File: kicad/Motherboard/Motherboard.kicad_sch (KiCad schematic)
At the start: 64 parts, among them J1 USB_C_Receptacle_USB2.0, J2 Conn_01x16_Pin, J3 Conn_01x16_Pin, J4 Conn_01x16_Pin, J5 Conn_01x02_Pin, J6 Conn_01x04_Pin, J7 Conn_01x04_Pin, J8 Conn_01x16_Pin, J9 Conn_01x02_Pin, Q1 DMN3404L, SW1 Reset, SW2 Boot, U1 ESP32-S2-SOLO, U2 LD1117S33TR_SOT223, U3 CD74HC4067M, U4 CD74HC4067M, U5 CD74HC4067M, U6 CD74HC4067M, U7 TMC2208-LA, U8 TMC2208-LA, U9 LM2575-5.0BT

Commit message: final schematic
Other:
- moved on the sheet: TP1
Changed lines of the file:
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@@
 	)
 	(junction
+		(at 30.48 176.53)
+		(diameter 0)
+		(color 0 0 0 0)
+	)
+	(junction
 		(at 81.28 148.59)
 		(diameter 0)
@@
 	)
 	(junction
-		(at 34.29 176.53)
-		(diameter 0)
-		(color 0 0 0 0)
-	)
-	(junction
 		(at 87.63 148.59)
 		(diameter 0)
@@
 	(wire
 		(pts
-			(xy 34.29 176.53) (xy 35.56 176.53)
-		)
-		(stroke
-			(width 0)
-			(type default)
-		)
-	)
-	(wire
-		(pts
 			(xy 92.71 177.8) (xy 96.52 177.8)
 		)
@@
 	(wire
 		(pts
-			(xy 29.21 176.53) (xy 34.29 176.53)
+			(xy 29.21 176.53) (xy 30.48 176.53)
 		)
 		(stroke
@@
 	(wire
 		(pts
+			(xy 30.48 176.53) (xy 35.56 176.53)
+		)
+		(stroke
+			(width 0)
+			(type default)
+		)
+	)
+	(wire
+		(pts
 			(xy 191.77 27.94) (xy 191.77 29.21)
 		)
@@
 		(on_board yes)
 		(dnp no)
-		(fields_autoplaced yes)
 		(property "Reference" "TP2"
-			(at 118.11 173.2279 0)
+			(at 113.792 172.466 0)
 			(effects
 				(font
@@
 		)
 		(property "Value" "12VConverter_TestPoint"
-			(at 118.11 175.7679 0)
+			(at 100.33 170.434 0)
 			(effects
 				(font
@@
 		(dnp no)
 		(property "Reference" "D2"
-			(at 137.16 176.53 90)
+			(at 143.256 175.514 0)
 			(effects
 				(font
@@
 		)
 		(property "Value" "1N5819"
-			(at 145.542 180.848 0)
+			(at 147.066 174.498 90)
 			(effects
 				(font
@@
 		(on_board yes)
 		(dnp no)
-		(fields_autoplaced yes)
 		(property "Reference" "TP3"
-			(at 138.43 176.0219 0)
+			(at 134.112 179.578 0)
 			(effects
 				(font
@@
 		)
 		(property "Value" "BeforeEM_TestPoint"
-			(at 138.43 178.5619 0)
+			(at 126.492 181.61 0)
 			(effects
 				(font
@@
 		(on_board yes)
 		(dnp no)
-		(fields_autoplaced yes)
 		(property "Reference" "#PWR034"
 			(at 35.56 180.34 0)
@@
 		)
 		(property "Value" "+12V"
-			(at 35.56 171.45 0)
+			(at 38.862 174.752 0)
 			(effects
 				(font
@@
 		(on_board yes)
 		(dnp no)
-		(fields_autoplaced yes)
 		(property "Reference" "#FLG02"
 			(at 118.11 175.895 0)
@@
 		)
 		(property "Value" "PWR_FLAG"
-			(at 118.11 172.72 0)
+			(at 123.952 174.752 0)
 			(effects
 				(font
@@
 		)
 		(property "Value" "DMN3404L"
-			(at 163.576 170.18 90)
+			(at 157.734 184.15 0)
 			(effects
 				(font
@@
 		)
 		(property "Value" "GND"
-			(at 53.34 138.43 90)
+			(at 57.15 135.382 90)
 			(effects
 				(font
@@
 		)
 		(property "Value" "GND"
-			(at 127 138.43 90)
+			(at 130.81 135.382 90)
 			(effects
 				(font
@@
 		(on_board yes)
 		(dnp no)
-		(fields_autoplaced yes)
 		(property "Reference" "TP4"
-			(at 163.83 169.4179 0)
+			(at 159.512 168.91 0)
 			(effects
 				(font
@@
 		)
 		(property "Value" "AfterEM_TestPoint"
-			(at 163.83 171.9579 0)
+			(at 152.654 166.624 0)
 			(effects
 				(font
@@
 		(on_board yes)
 		(dnp no)
-		(fields_autoplaced yes)
 		(property "Reference" "TP6"
-			(at 132.08 142.7479 0)
+			(at 124.46 144.018 0)
 			(effects
 				(font
@@
 		)
 		(property "Value" "TMC_Input1_TestPoint"
-			(at 132.08 145.2879 0)
+			(at 119.38 141.732 0)
 			(effects
 				(font
@@
 		(on_board yes)
 		(dnp no)
-		(fields_autoplaced yes)
 		(property "Reference" "TP5"
-			(at 220.98 137.1599 90)
+			(at 220.218 138.684 90)
 			(effects
 				(font
@@
 		)
 		(property "Value" "3.3VConverter_TestPoint"
-			(at 220.98 139.6999 90)
+			(at 204.216 148.336 90)
 			(effects
 				(font
@@
 		(on_board yes)
 		(dnp no)
-		(fields_autoplaced yes)
 		(property "Reference" "J9"
-			(at 24.765 171.45 0)
+			(at 24.13 174.498 0)
 			(effects
 				(font
@@
 		)
 		(property "Value" "Conn_01x02_Pin"
-			(at 24.765 173.99 0)
+			(at 24.13 180.594 0)
 			(effects
 				(font
@@
 		(on_board yes)
 		(dnp no)
-		(fields_autoplaced yes)
 		(property "Reference" "TP7"
-			(at 57.15 144.0179 0)
+			(at 49.53 145.542 0)
 			(effects
 				(font
@@
 		)
 		(property "Value" "TMC_Input2_TestPoint"
-			(at 57.15 146.5579 0)
+			(at 44.196 143.002 0)
 			(effects
 				(font
@@
 	(symbol
 		(lib_id "Connector:TestPoint")
-		(at 34.29 176.53 0)
+		(at 30.48 176.53 0)
 		(unit 1)
 		(exclude_from_sim no)
@@
 		(on_board yes)
 		(dnp no)
-		(fields_autoplaced yes)
 		(property "Reference" "TP1"
-			(at 36.83 171.9579 0)
+			(at 28.448 171.196 0)
 			(effects
 				(font
@@
 		)
 		(property "Value" "PowerSupply_TestPoint"
-			(at 36.83 174.4979 0)
+			(at 19.558 168.91 0)
 			(effects
 				(font
@@
 		)
 		(property "Footprint" "TestPoint:TestPoint_Pad_1.5x1.5mm"
-			(at 39.37 176.53 0)
+			(at 35.56 176.53 0)
 			(effects
 				(font
@@
 		)
 		(property "Datasheet" "~"
-			(at 39.37 176.53 0)
+			(at 35.56 176.53 0)
 			(effects
 				(font
@@
 		)
 		(property "Description" "test point"
-			(at 34.29 176.53 0)
+			(at 30.48 176.53 0)
 			(effects
 				(font

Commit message: Final Schem done
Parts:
- removed J2, J3, J4, J8: Conn_01x16_Pin, Connector_PinHeader_2.54mm:PinHeader_1x16_P2.54mm_Vertical, symbol Connector:Conn_01x16_Pin
- removed U3, U4, U5, U6: CD74HC4067M, Package_SO:SOIC-24W_7.5x15.4mm_P1.27mm, symbol 74xx:CD74HC4067M
- added J10, J11, J12, J13, J14, J15, J16, J17: Conn_01x08_Pin, Connector_PinHeader_2.54mm:PinHeader_1x08_P2.54mm_Vertical, symbol Connector:Conn_01x08_Pin
- added R10, R11, R12, R13, R14, R15, R16, R17: 10k, Resistor_SMD:R_0805_2012Metric_Pad1.20x1.40mm_HandSolder, symbol Device:R
- added U3, U4, U5, U6: TCA9535RTWR, Package_DFN_QFN:WQFN-24-1EP_4x4mm_P0.5mm_EP2.45x2.45mm, symbol Interface_Expansion:TCA9535RTWR
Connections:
- net bit0 is gone; now on net +3.3V: U1.39 (GPIO1/TOUCH1/ADC1_CH0)
- net +3.3V: now also R10.1, R11.1, R12.1, R12.2, R13.1, R13.2, R14.1, R15.1, R15.2, R16.1, R17.1, R17.2, U3.20 (SDA), U3.21 (VCC), U4.20 (SDA), U4.21 (VCC), U4.24 (A2), U5.20 (SDA), U5.21 (VCC), U5.23 (A1), U6.18 (A0), U6.20 (SDA), U6.21 (VCC)
- net GND: now also U3.18 (A0), U3.23 (A1), U3.24 (A2), U3.25 (EPAD), U3.9 (GND), U4.18 (A0), U4.23 (A1), U4.25 (EPAD), U4.9 (GND), U5.18 (A0), U5.24 (A2), U5.25 (EPAD), U5.9 (GND), U6.23 (A1), U6.24 (A2), U6.25 (EPAD), U6.9 (GND)
- net COM0: no longer names the net of U1.6 (GPIO6/TOUCH6/ADC1_CH5)
- net COM1: no longer names the net of U1.12 (GPIO8/TOUCH8/ADC1_CH7)
- net COM2: no longer names the net of U1.18 (GPIO10/TOUCH10/ADC1_CH9/FSPICS0/FSPIIO4)
- net COM3: no longer names the net of U1.20 (GPIO12/TOUCH12/ADC2_CH1/FSPICLK/FSPIIO6)
- net EN0: no longer names the net of U1.5 (GPIO5/TOUCH5/ADC1_CH4)
- net EN1: no longer names the net of U1.7 (GPIO7/TOUCH7/ADC1_CH6)
- net EN2: no longer names the net of U1.17 (GPIO9/TOUCH9/ADC1_CH8/FSPIHD)
- net EN3: no longer names the net of U1.19 (GPIO11/TOUCH11/ADC2_CH0/FSPID/FSPIIO5)
- net bit1 renamed SCL
- net SCL: now also R10.2, R11.2, R14.2, R16.2, U3.19 (SCL), U4.19 (SCL), U5.19 (SCL), U6.19 (SCL)
- net bit2: no longer names the net of U1.15 (GPIO3/TOUCH3/ADC1_CH2)
- net bit3: no longer names the net of U1.4 (GPIO4/TOUCH4/ADC1_CH3)
- new net: J10.1 (Pin_1), U3.8 (P07)
- new net: J10.2 (Pin_2), U3.7 (P06)
- new net: J10.3 (Pin_3), U3.6 (P05)
- new net: J10.4 (Pin_4), U3.5 (P04)
- new net: J10.5 (Pin_5), U3.4 (P03)
- new net: J10.6 (Pin_6), U3.3 (P02)
- new net: J10.7 (Pin_7), U3.2 (P01)
- new net: J10.8 (Pin_8), U3.1 (P00)
- new net: J14.1 (Pin_1), U5.8 (P07)
- new net: J14.2 (Pin_2), U5.7 (P06)
- new net: J14.3 (Pin_3), U5.6 (P05)
- new net: J14.4 (Pin_4), U5.5 (P04)
- new net: J14.5 (Pin_5), U5.4 (P03)
- new net: J14.6 (Pin_6), U5.3 (P02)
- new net: J14.7 (Pin_7), U5.2 (P01)
- new net: J14.8 (Pin_8), U5.1 (P00)
- new net: J12.8 (Pin_8), U4.1 (P00)
- new net: J13.8 (Pin_8), U4.10 (P10)
- new net: J13.7 (Pin_7), U4.11 (P11)
- new net: J13.6 (Pin_6), U4.12 (P12)
- new net: J13.5 (Pin_5), U4.13 (P13)
- new net: J13.4 (Pin_4), U4.14 (P14)
- new net: J13.3 (Pin_3), U4.15 (P15)
- new net: J13.2 (Pin_2), U4.16 (P16)
- new net: J13.1 (Pin_1), U4.17 (P17)
- new net: J12.7 (Pin_7), U4.2 (P01)
- new net: J12.6 (Pin_6), U4.3 (P02)
- new net: J12.5 (Pin_5), U4.4 (P03)
- new net: J12.4 (Pin_4), U4.5 (P04)
- new net: J12.3 (Pin_3), U4.6 (P05)
- new net: J12.2 (Pin_2), U4.7 (P06)
- new net: J12.1 (Pin_1), U4.8 (P07)
- new net: J16.8 (Pin_8), U6.1 (P00)
- new net: J17.8 (Pin_8), U6.10 (P10)
- new net: J17.7 (Pin_7), U6.11 (P11)
- new net: J17.6 (Pin_6), U6.12 (P12)
- new net: J17.5 (Pin_5), U6.13 (P13)
- new net: J17.4 (Pin_4), U6.14 (P14)
- new net: J17.3 (Pin_3), U6.15 (P15)
- new net: J17.2 (Pin_2), U6.16 (P16)
- new net: J17.1 (Pin_1), U6.17 (P17)
- new net: J16.7 (Pin_7), U6.2 (P01)
- new net: J16.6 (Pin_6), U6.3 (P02)
- new net: J16.5 (Pin_5), U6.4 (P03)
- new net: J16.4 (Pin_4), U6.5 (P04)
- new net: J16.3 (Pin_3), U6.6 (P05)
- new net: J16.2 (Pin_2), U6.7 (P06)
- new net: J16.1 (Pin_1), U6.8 (P07)
- new net: J15.8 (Pin_8), U5.10 (P10)
- new net: J15.7 (Pin_7), U5.11 (P11)
- new net: J15.6 (Pin_6), U5.12 (P12)
- new net: J15.5 (Pin_5), U5.13 (P13)
- new net: J15.4 (Pin_4), U5.14 (P14)
- new net: J15.3 (Pin_3), U5.15 (P15)
- new net: J15.2 (Pin_2), U5.16 (P16)
- new net: J15.1 (Pin_1), U5.17 (P17)
- new net: J11.1 (Pin_1), U3.17 (P17)
- new net: J11.2 (Pin_2), U3.16 (P16)
- new net: J11.3 (Pin_3), U3.15 (P15)
- new net: J11.4 (Pin_4), U3.14 (P14)
- new net: J11.5 (Pin_5), U3.13 (P13)
- new net: J11.6 (Pin_6), U3.12 (P12)
- new net: J11.7 (Pin_7), U3.11 (P11)
- new net: J11.8 (Pin_8), U3.10 (P10)
- no-connect marks 28 -> 42

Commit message: finalized schematic
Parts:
- removed TP3: BeforeEM_TestPoint, TestPoint:TestPoint_Pad_1.5x1.5mm, symbol Connector:TestPoint
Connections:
- net GND is gone; now on net +3.3V: C1.1, C10.2, C11.2, C13.1, C14.1, C15.1, C19.1, C2.1, C20.2, C21.1, C22.2, C23.1, C24.2, C3.2, C4.1, C5.2, C6.2, C7.2, C8.2, C9.2, D1.2 (A), J1.A1 (GND), J1.A12 (GND), J1.B1 (GND), J1.B12 (GND), J1.S1 (SHIELD), J9.2 (Pin_2), Q1.2 (S), R1.1, R3.2, R5.1, R6.1, R7.1, R8.1, R9.1, SW1.1, SW2.2, TP4.1, U1.1 (GND), U1.40 (GND), U1.41 (GND), U2.1 (GND), U3.18 (A0), U3.23 (A1), U3.24 (A2), U3.25 (EPAD), U3.9 (GND), U4.18 (A0), U4.23 (A1), U4.25 (EPAD), U4.9 (GND), U5.18 (A0), U5.24 (A2), U5.25 (EPAD), U5.9 (GND), U6.23 (A1), U6.24 (A2), U6.25 (EPAD), U6.9 (GND), U7.18 (GND), U7.3 (GND), U8.18 (GND), U8.3 (GND), U9.3 (GND), U9.5 (~{ON}/OFF)
- net +3.3V: no longer R12.2, R13.2, R15.2, R17.2, U1.39 (GPIO1/TOUCH1/ADC1_CH0), U3.20 (SDA), U4.20 (SDA), U5.20 (SDA), U6.20 (SDA)
- net D+: now also U1.14 (GPIO20/U1CTS/ADC2_CH9/CLK_OUT1/USB_D+)
- net D-: now also U1.13 (GPIO19/U1RTS/ADC2_CH8/CLK_OUT2/USB_D-)
- net DIR_1: now also U1.38 (GPIO2/TOUCH2/ADC1_CH1); no longer U1.22 (GPIO14/TOUCH14/ADC2_CH3/FSPIWP/FSPIDQS)
- net DIR_2: now also U1.5 (GPIO5/TOUCH5/ADC1_CH4); no longer U1.24 (SPIIO4/GPIO33/FSPIHD)
- net ENN_1: now also U1.39 (GPIO1/TOUCH1/ADC1_CH0); no longer U1.21 (GPIO13/TOUCH13/ADC2_CH2/FSPIQ/FSPIIO7)
- net ENN_2: now also U1.4 (GPIO4/TOUCH4/ADC1_CH3); no longer U1.23 (GPIO21)
- net MAGCT: now also U1.18 (GPIO10/TOUCH10/ADC1_CH9/FSPICS0/FSPIIO4); no longer U1.29 (SPIIO7/GPIO36/FSPICLK)
- net SCL: now also R12.2, R13.2, R15.2, R17.2, U1.24 (SPIIO4/GPIO33/FSPIHD), U1.25 (SPIIO5/GPIO34/FSPICS0), U3.20 (SDA), U4.20 (SDA), U5.20 (SDA), U6.20 (SDA); no longer U1.38 (GPIO2/TOUCH2/ADC1_CH1)
- net STEP_1: now also U1.15 (GPIO3/TOUCH3/ADC1_CH2); no longer U1.10 (GPIO17/U1TXD/ADC2_CH6/DAC_1)
- net STEP_2: now also U1.6 (GPIO6/TOUCH6/ADC1_CH5); no longer U1.25 (SPIIO5/GPIO34/FSPICS0)
- net UART_1: now also U1.36 (U0RXD/GPIO44/CLK_OUT2); no longer U1.11 (GPIO18/U1RXD/ADC2_CH7/DAC_2/CLK_OUT3)
- net UART_2: now also U1.37 (U0TXD/GPIO43/CLK_OUT1); no longer U1.28 (SPIIO6/GPIO35/FSPID)
- no-connect marks 42 -> 40
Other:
- moved on the sheet: C10, C11, C12, C13, C14, C15, C16, C17, C18, C19, C20, C21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

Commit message: fixed schematic
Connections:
- net +3.3V: no longer C1.1, C10.2, C11.2, C13.1, C14.1, C15.1, C19.1, C2.1, C20.2, C21.1, C22.2, C23.1, C24.2, C3.2, C4.1, C5.2, C6.2, C7.2, C8.2, C9.2, D1.2 (A), J1.A1 (GND), J1.A12 (GND), J1.B1 (GND), J1.B12 (GND), J1.S1 (SHIELD), J9.2 (Pin_2), Q1.2 (S), R1.1, R3.2, R5.1, R6.1, R7.1, R8.1, R9.1, SW1.1, SW2.2, TP4.1, U1.1 (GND), U1.40 (GND), U1.41 (GND), U2.1 (GND), U3.18 (A0), U3.23 (A1), U3.24 (A2), U3.25 (EPAD), U3.9 (GND), U4.18 (A0), U4.23 (A1), U4.25 (EPAD), U4.9 (GND), U5.18 (A0), U5.24 (A2), U5.25 (EPAD), U5.9 (GND), U6.23 (A1), U6.24 (A2), U6.25 (EPAD), U6.9 (GND), U7.18 (GND), U7.3 (GND), U8.18 (GND), U8.3 (GND), U9.3 (GND), U9.5 (~{ON}/OFF)
- net SCL: no longer R12.2, R13.2, R15.2, R17.2, U1.24 (SPIIO4/GPIO33/FSPIHD), U3.20 (SDA), U4.20 (SDA), U5.20 (SDA), U6.20 (SDA)
- new net GND: C1.1, C10.2, C11.2, C13.1, C14.1, C15.1, C19.1, C2.1, C20.2, C21.1, C22.2, C23.1, C24.2, C3.2, C4.1, C5.2, C6.2, C7.2, C8.2, C9.2, D1.2 (A), J1.A1 (GND), J1.A12 (GND), J1.B1 (GND), J1.B12 (GND), J1.S1 (SHIELD), J9.2 (Pin_2), Q1.2 (S), R1.1, R3.2, R5.1, R6.1, R7.1, R8.1, R9.1, SW1.1, SW2.2, TP4.1, U1.1 (GND), U1.40 (GND), U1.41 (GND), U2.1 (GND), U3.18 (A0), U3.23 (A1), U3.24 (A2), U3.25 (EPAD), U3.9 (GND), U4.18 (A0), U4.23 (A1), U4.25 (EPAD), U4.9 (GND), U5.18 (A0), U5.24 (A2), U5.25 (EPAD), U5.9 (GND), U6.23 (A1), U6.24 (A2), U6.25 (EPAD), U6.9 (GND), U7.18 (GND), U7.3 (GND), U8.18 (GND), U8.3 (GND), U9.3 (GND), U9.5 (~{ON}/OFF)
- new net SDA: R12.2, R13.2, R15.2, R17.2, U1.24 (SPIIO4/GPIO33/FSPIHD), U3.20 (SDA), U4.20 (SDA), U5.20 (SDA), U6.20 (SDA)
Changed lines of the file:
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@@
 	)
 	(junction
-		(at 78.74 22.86)
-		(diameter 0)
-		(color 0 0 0 0)
-	)
-	(junction
 		(at 52.07 172.72)
 		(diameter 0)
@@
 	)
 	(junction
-		(at 22.86 24.13)
-		(diameter 0)
-		(color 0 0 0 0)
-	)
-	(junction
 		(at 270.51 20.32)
 		(diameter 0)
@@
 	)
 	(junction
-		(at 25.4 124.46)
-		(diameter 0)
-		(color 0 0 0 0)
-	)
-	(junction
 		(at 25.4 64.77)
 		(diameter 0)
@@
 	)
 	(junction
-		(at 22.86 83.82)
-		(diameter 0)
-		(color 0 0 0 0)
-	)
-	(junction
-		(at 135.89 24.13)
-		(diameter 0)
-		(color 0 0 0 0)
-	)
-	(junction
 		(at 138.43 24.13)
 		(diameter 0)
@@
 	)
 	(junction
+		(at 34.29 182.88)
+		(diameter 0)
+		(color 0 0 0 0)
+	)
+	(junction
 		(at 254 162.56)
 		(diameter 0)
@@
 	)
 	(junction
-		(at 138.43 62.23)
-		(diameter 0)
-		(color 0 0 0 0)
-	)
-	(junction
 		(at 96.52 134.62)
 		(diameter 0)
@@
 	(wire
 		(pts
-			(xy 25.4 124.46) (xy 25.4 132.08)
-		)
-		(stroke
-			(width 0)
-			(type default)
-		)
-	)
-	(wire
-		(pts
 			(xy 92.71 177.8) (xy 96.52 177.8)
 		)
@@
 	(wire
 		(pts
-			(xy 138.43 59.69) (xy 138.43 62.23)
+			(xy 34.29 180.34) (xy 29.21 180.34)
+		)
+		(stroke
+			(width 0)
+			(type default)
+		)
+	)
+	(wire
+		(pts
+			(xy 138.43 59.69) (xy 138.43 64.77)
 		)
 		(stroke
@@
 	(wire
 		(pts
-			(xy 135.89 24.13) (xy 138.43 24.13)
+			(xy 133.35 24.13) (xy 138.43 24.13)
 		)
 		(stroke
@@
 	(wire
 		(pts
-			(xy 29.21 180.34) (xy 35.56 180.34)
-		)
-		(stroke
-			(width 0)
-			(type default)
-		)
-	)
-	(wire
-		(pts
-			(xy 22.86 24.13) (xy 25.4 24.13)
-		)
-		(stroke
-			(width 0)
-			(type default)
-		)
-	)
-	(wire
-		(pts
 			(xy 25.4 86.36) (xy 22.86 86.36)
 		)
@@
 	(wire
 		(pts
-			(xy 25.4 121.92) (xy 25.4 124.46)
+			(xy 25.4 121.92) (xy 25.4 132.08)
 		)
 		(stroke
@@
 	(wire
 		(pts
-			(xy 133.35 24.13) (xy 135.89 24.13)
-		)
-		(stroke
-			(width 0)
-			(type default)
-		)
-	)
-	(wire
-		(pts
 			(xy 191.77 27.94) (xy 191.77 29.21)
 		)
@@
 	(wire
 		(pts
-			(xy 22.86 83.82) (xy 25.4 83.82)
-		)
-		(stroke
-			(width 0)
-			(type default)
-		)
-	)
-	(wire
-		(pts
 			(xy 161.29 173.99) (xy 158.75 173.99)
 		)
@@
 	(wire
 		(pts
-			(xy 20.32 24.13) (xy 22.86 24.13)
+			(xy 20.32 24.13) (xy 25.4 24.13)
 		)
 		(stroke
@@
 	(wire
 		(pts
-			(xy 78.74 22.86) (xy 81.28 22.86)
+			(xy 76.2 22.86) (xy 81.28 22.86)
 		)
 		(stroke
@@
 	(wire
 		(pts
+			(xy 34.29 182.88) (xy 34.29 180.34)
+		)
+		(stroke
+			(width 0)
+			(type default)
+		)
+	)
+	(wire
+		(pts
 			(xy 118.11 177.8) (xy 120.65 177.8)
 		)
@@
 	(wire
 		(pts
-			(xy 138.43 62.23) (xy 138.43 64.77)
-		)
-		(stroke
-			(width 0)
-			(type default)
-		)
-	)
-	(wire
-		(pts
 			(xy 67.31 177.8) (xy 67.31 185.42)
 		)
@@
 	(wire
 		(pts
-			(xy 76.2 22.86) (xy 78.74 22.86)
-		)
-		(stroke
-			(width 0)
-			(type default)
-		)
-	)
-	(wire
-		(pts
 			(xy 138.43 173.99) (xy 138.43 177.8)
 		)
@@
 	(wire
 		(pts
+			(xy 34.29 182.88) (xy 34.29 185.42)
+		)
+		(stroke
+			(width 0)
+			(type default)
+		)
+	)
+	(wire
+		(pts
 			(xy 76.2 101.6) (xy 80.01 101.6)
 		)
@@
 	(wire
 		(pts
-			(xy 20.32 83.82) (xy 22.86 83.82)
+			(xy 20.32 83.82) (xy 25.4 83.82)
 		)
 		(stroke
@@
 		(lib_name "GND_1")
 		(lib_id "power:GND")
-		(at 35.56 180.34 0)
+		(at 34.29 185.42 0)
 		(unit 1)
 		(exclude_from_sim no)
@@
 		(fields_autoplaced yes)
 		(property "Reference" "#PWR035"
-			(at 35.56 186.69 0)
+			(at 34.29 191.77 0)
 			(effects
 				(font
@@
 		)
 		(property "Value" "GND"
-			(at 35.56 185.42 0)
+			(at 34.29 190.5 0)
 			(effects
 				(font
@@
 		)
 		(property "Footprint" ""
-			(at 35.56 180.34 0)
+			(at 34.29 185.42 0)
 			(effects
 				(font
@@
 		)
 		(property "Datasheet" ""
-			(at 35.56 180.34 0)
+			(at 34.29 185.42 0)
 			(effects
 				(font
@@
 		)
 		(property "Description" "Power symbol creates a global label with name \"GND\" , ground"
-			(at 35.56 180.34 0)
+			(at 34.29 185.42 0)
 			(effects
 				(font
@@
 					(unit 1)
 				)
+			)
+		)
+	)
+	(symbol
+		(lib_id "power:PWR_FLAG")
+		(at 34.29 182.88 270)
+		(unit 1)
+		(exclude_from_sim no)
+		(in_bom yes)
+		(on_board yes)
+		(dnp no)
+		(property "Reference" "#FLG03"
+			(at 36.195 182.88 0)
+			(effects
+				(font
+					(size 1.27 1.27)
+				)
+				(hide yes)
+			)
+		)
+		(property "Value" "PWR_FLAG"
+			(at 38.1 178.562 0)
+			(effects
+				(font
+					(size 1.27 1.27)
+				)
+				(justify left)
+			)
+		)
+		(property "Footprint" ""
+			(at 34.29 182.88 0)
+			(effects
+				(font
+					(size 1.27 1.27)
+				)
+				(hide yes)
+			)
+		)
+		(property "Datasheet" "~"
+			(at 34.29 182.88 0)
+			(effects
+				(font
+					(size 1.27 1.27)
+				)
+				(hide yes)
+			)
+		)
+		(property "Description" "Special symbol for telling ERC where power comes from"
+			(at 34.29 182.88 0)
+			(effects
+				(font
+					(size 1.27 1.27)
+				)
+				(hide yes)
+			)
+		)
+		(pin "1"
+		)
+		(instances
+			(project ""
+				(path "/6e7606c8-26d5-4d26-b509-210c4758a44d"
+					(reference "#FLG03")
+					(unit 1)
+				)

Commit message: random sh
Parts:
- removed R12, R13, R14, R15, R16, R17: 10k, Resistor_SMD:R_0805_2012Metric_Pad1.20x1.40mm_HandSolder, symbol Device:R
- renumbered J14 to J10, J15 to J11, J16 to J12, J17 to J13, J5 to J2, J6 to J3, J7 to J4, J9 to J5, J10 to J6, J11 to J7, J12 to J8, J13 to J9
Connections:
- net SCL: no longer R11.2
- net SDA: now also R11.2
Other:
- moved on the sheet: C1, C2, C4, C5, J10, J11, J6, J7, R2, SW1, SW2, U1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

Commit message: fixed layout
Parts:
- removed TP4: AfterEM_TestPoint, TestPoint:TestPoint_Pad_1.5x1.5mm, symbol Connector:TestPoint
- added F1: Polyfuse, symbol Device:Polyfuse
- renumbered TP5 to TP3, TP6 to TP4, TP7 to TP5
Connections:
- net +12V: now also F1.2; no longer J5.1 (Pin_1), TP1.1
- new net: F1.1, J5.1 (Pin_1), TP1.1
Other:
- moved on the sheet: J5, TP1

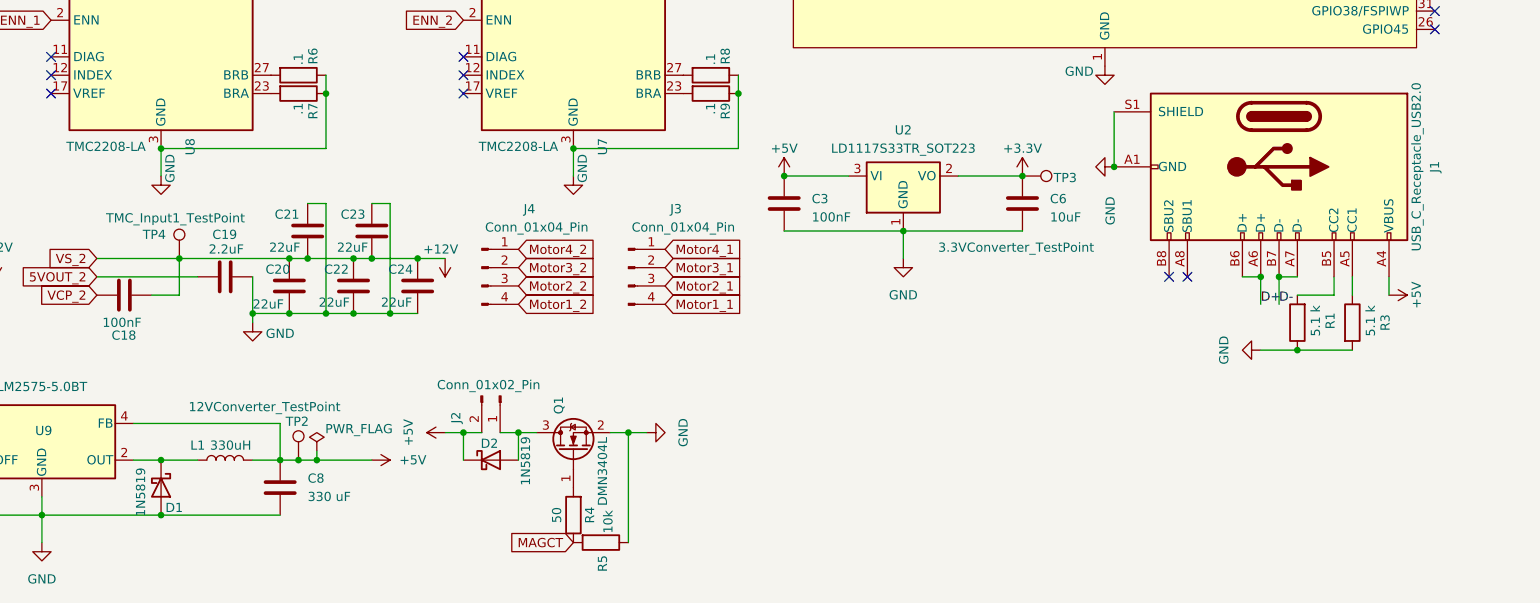
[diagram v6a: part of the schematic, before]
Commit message: finalized schematic
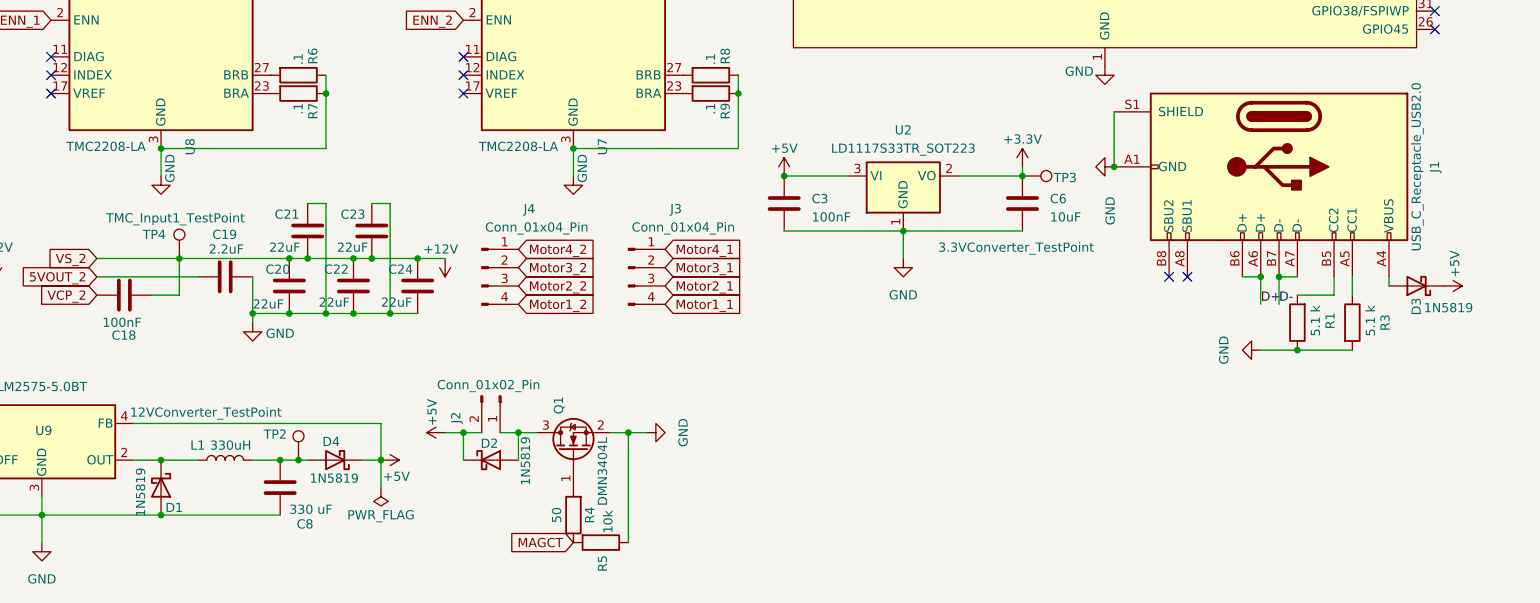
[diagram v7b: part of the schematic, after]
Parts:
- added D3, D4: 1N5819, Diode_THT:D_DO-41_SOD81_P5.08mm_Vertical_AnodeUp, symbol Device:D_Schottky
- F1: footprint (none) -> Fuse:Fuse_2920_7451Metric_Pad2.10x5.45mm_HandSolder
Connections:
- net +5V: now also D3.1 (K), D4.1 (K); no longer C8.1, J1.A4 (VBUS), J1.A9 (VBUS), J1.B4 (VBUS), J1.B9 (VBUS), L1.2, TP2.1
- new net: C8.1, D4.2 (A), L1.2, TP2.1
- new net: D3.2 (A), J1.A4 (VBUS), J1.A9 (VBUS), J1.B4 (VBUS), J1.B9 (VBUS)
